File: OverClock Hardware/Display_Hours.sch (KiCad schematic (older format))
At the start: 40 parts, among them U3 10M02SCE144

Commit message: Completed Initial Routing
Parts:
- R11, R12, R13, R14, R15, R16, R17, R18, R19, R20, R21, R22, R23, R24, R25, R26: footprint Resistor_SMD:R_0805_2012Metric_Pad1.15x1.40mm_HandSolder -> Resistor_SMD:R_0603_1608Metric_Pad1.05x0.95mm_HandSolder
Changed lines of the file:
@@
 F 0 "R11" H 10909 5346 50  0000 L CNN
 F 1 "1K" H 10909 5255 50  0000 L CNN
-F 2 "Resistor_SMD:R_0805_2012Metric_Pad1.15x1.40mm_HandSolder" H 10850 5300 50  0001 C CNN
+F 2 "Resistor_SMD:R_0603_1608Metric_Pad1.05x0.95mm_HandSolder" H 10850 5300 50  0001 C CNN
 F 3 "~" H 10850 5300 50  0001 C CNN
 	1    10850 5300
@@
 F 0 "R12" H 11459 5346 50  0000 L CNN
 F 1 "1K" H 11459 5255 50  0000 L CNN
-F 2 "Resistor_SMD:R_0805_2012Metric_Pad1.15x1.40mm_HandSolder" H 11400 5300 50  0001 C CNN
+F 2 "Resistor_SMD:R_0603_1608Metric_Pad1.05x0.95mm_HandSolder" H 11400 5300 50  0001 C CNN
 F 3 "~" H 11400 5300 50  0001 C CNN
 	1    11400 5300
@@
 F 0 "R13" H 12009 5346 50  0000 L CNN
 F 1 "1K" H 12009 5255 50  0000 L CNN
-F 2 "Resistor_SMD:R_0805_2012Metric_Pad1.15x1.40mm_HandSolder" H 11950 5300 50  0001 C CNN
+F 2 "Resistor_SMD:R_0603_1608Metric_Pad1.05x0.95mm_HandSolder" H 11950 5300 50  0001 C CNN
 F 3 "~" H 11950 5300 50  0001 C CNN
 	1    11950 5300
@@
 F 0 "R14" H 12559 5346 50  0000 L CNN
 F 1 "1K" H 12559 5255 50  0000 L CNN
-F 2 "Resistor_SMD:R_0805_2012Metric_Pad1.15x1.40mm_HandSolder" H 12500 5300 50  0001 C CNN
+F 2 "Resistor_SMD:R_0603_1608Metric_Pad1.05x0.95mm_HandSolder" H 12500 5300 50  0001 C CNN
 F 3 "~" H 12500 5300 50  0001 C CNN
 	1    12500 5300
@@
 F 0 "R15" H 13109 5346 50  0000 L CNN
 F 1 "1K" H 13109 5255 50  0000 L CNN
-F 2 "Resistor_SMD:R_0805_2012Metric_Pad1.15x1.40mm_HandSolder" H 13050 5300 50  0001 C CNN
+F 2 "Resistor_SMD:R_0603_1608Metric_Pad1.05x0.95mm_HandSolder" H 13050 5300 50  0001 C CNN
 F 3 "~" H 13050 5300 50  0001 C CNN
 	1    13050 5300
@@
 F 0 "R16" H 13659 5346 50  0000 L CNN
 F 1 "1K" H 13659 5255 50  0000 L CNN
-F 2 "Resistor_SMD:R_0805_2012Metric_Pad1.15x1.40mm_HandSolder" H 13600 5300 50  0001 C CNN
+F 2 "Resistor_SMD:R_0603_1608Metric_Pad1.05x0.95mm_HandSolder" H 13600 5300 50  0001 C CNN
 F 3 "~" H 13600 5300 50  0001 C CNN
 	1    13600 5300
@@
 F 0 "R17" H 14209 5346 50  0000 L CNN
 F 1 "1K" H 14209 5255 50  0000 L CNN
-F 2 "Resistor_SMD:R_0805_2012Metric_Pad1.15x1.40mm_HandSolder" H 14150 5300 50  0001 C CNN
+F 2 "Resistor_SMD:R_0603_1608Metric_Pad1.05x0.95mm_HandSolder" H 14150 5300 50  0001 C CNN
 F 3 "~" H 14150 5300 50  0001 C CNN
 	1    14150 5300
@@
 F 0 "R18" H 14809 5346 50  0000 L CNN
 F 1 "1K" H 14809 5255 50  0000 L CNN
-F 2 "Resistor_SMD:R_0805_2012Metric_Pad1.15x1.40mm_HandSolder" H 14750 5300 50  0001 C CNN
+F 2 "Resistor_SMD:R_0603_1608Metric_Pad1.05x0.95mm_HandSolder" H 14750 5300 50  0001 C CNN
 F 3 "~" H 14750 5300 50  0001 C CNN
 	1    14750 5300
@@
 F 0 "R19" H 3759 5396 50  0000 L CNN
 F 1 "1K" H 3759 5305 50  0000 L CNN
-F 2 "Resistor_SMD:R_0805_2012Metric_Pad1.15x1.40mm_HandSolder" H 3700 5350 50  0001 C CNN
+F 2 "Resistor_SMD:R_0603_1608Metric_Pad1.05x0.95mm_HandSolder" H 3700 5350 50  0001 C CNN
 F 3 "~" H 3700 5350 50  0001 C CNN
 	1    3700 5350
@@
 F 0 "R20" H 4309 5396 50  0000 L CNN
 F 1 "1K" H 4309 5305 50  0000 L CNN
-F 2 "Resistor_SMD:R_0805_2012Metric_Pad1.15x1.40mm_HandSolder" H 4250 5350 50  0001 C CNN
+F 2 "Resistor_SMD:R_0603_1608Metric_Pad1.05x0.95mm_HandSolder" H 4250 5350 50  0001 C CNN
 F 3 "~" H 4250 5350 50  0001 C CNN
 	1    4250 5350
@@
 F 0 "R21" H 4859 5396 50  0000 L CNN
 F 1 "1K" H 4859 5305 50  0000 L CNN
-F 2 "Resistor_SMD:R_0805_2012Metric_Pad1.15x1.40mm_HandSolder" H 4800 5350 50  0001 C CNN
+F 2 "Resistor_SMD:R_0603_1608Metric_Pad1.05x0.95mm_HandSolder" H 4800 5350 50  0001 C CNN
 F 3 "~" H 4800 5350 50  0001 C CNN
 	1    4800 5350
@@
 F 0 "R22" H 5409 5396 50  0000 L CNN
 F 1 "1K" H 5409 5305 50  0000 L CNN
-F 2 "Resistor_SMD:R_0805_2012Metric_Pad1.15x1.40mm_HandSolder" H 5350 5350 50  0001 C CNN
+F 2 "Resistor_SMD:R_0603_1608Metric_Pad1.05x0.95mm_HandSolder" H 5350 5350 50  0001 C CNN
 F 3 "~" H 5350 5350 50  0001 C CNN
 	1    5350 5350
@@
 F 0 "R23" H 5959 5396 50  0000 L CNN
 F 1 "1K" H 5959 5305 50  0000 L CNN
-F 2 "Resistor_SMD:R_0805_2012Metric_Pad1.15x1.40mm_HandSolder" H 5900 5350 50  0001 C CNN
+F 2 "Resistor_SMD:R_0603_1608Metric_Pad1.05x0.95mm_HandSolder" H 5900 5350 50  0001 C CNN
 F 3 "~" H 5900 5350 50  0001 C CNN
 	1    5900 5350
@@
 F 0 "R24" H 6509 5396 50  0000 L CNN
 F 1 "1K" H 6509 5305 50  0000 L CNN
-F 2 "Resistor_SMD:R_0805_2012Metric_Pad1.15x1.40mm_HandSolder" H 6450 5350 50  0001 C CNN
+F 2 "Resistor_SMD:R_0603_1608Metric_Pad1.05x0.95mm_HandSolder" H 6450 5350 50  0001 C CNN
 F 3 "~" H 6450 5350 50  0001 C CNN
 	1    6450 5350
@@
 F 0 "R25" H 7059 5396 50  0000 L CNN
 F 1 "1K" H 7059 5305 50  0000 L CNN
-F 2 "Resistor_SMD:R_0805_2012Metric_Pad1.15x1.40mm_HandSolder" H 7000 5350 50  0001 C CNN
+F 2 "Resistor_SMD:R_0603_1608Metric_Pad1.05x0.95mm_HandSolder" H 7000 5350 50  0001 C CNN
 F 3 "~" H 7000 5350 50  0001 C CNN
 	1    7000 5350
@@
 F 0 "R26" H 7659 5396 50  0000 L CNN
 F 1 "1K" H 7659 5305 50  0000 L CNN
-F 2 "Resistor_SMD:R_0805_2012Metric_Pad1.15x1.40mm_HandSolder" H 7600 5350 50  0001 C CNN
+F 2 "Resistor_SMD:R_0603_1608Metric_Pad1.05x0.95mm_HandSolder" H 7600 5350 50  0001 C CNN
 F 3 "~" H 7600 5350 50  0001 C CNN
 	1    7600 5350

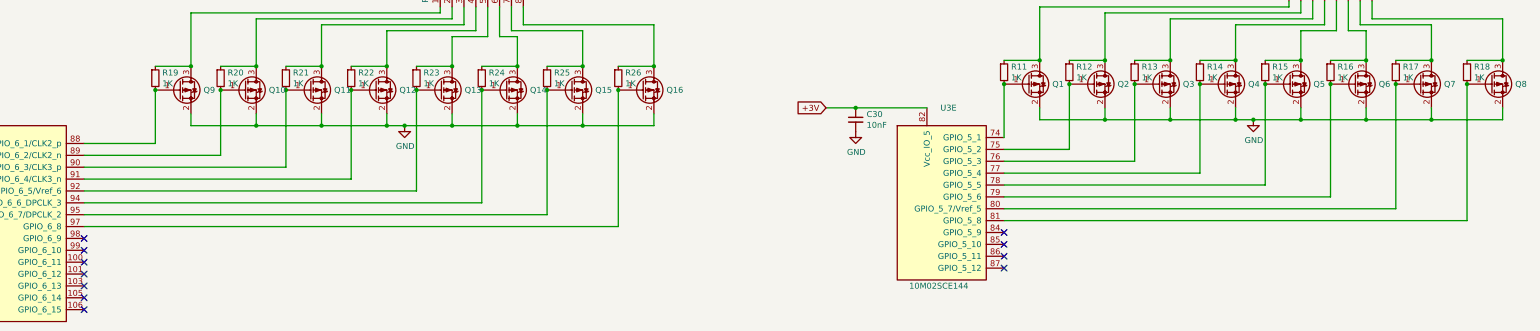
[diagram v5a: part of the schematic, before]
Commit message: Rerouted 7 Segment Displays
Rearranged the displays for cleaner routing, also modified the schematic for some of the displays to allow for better routing.
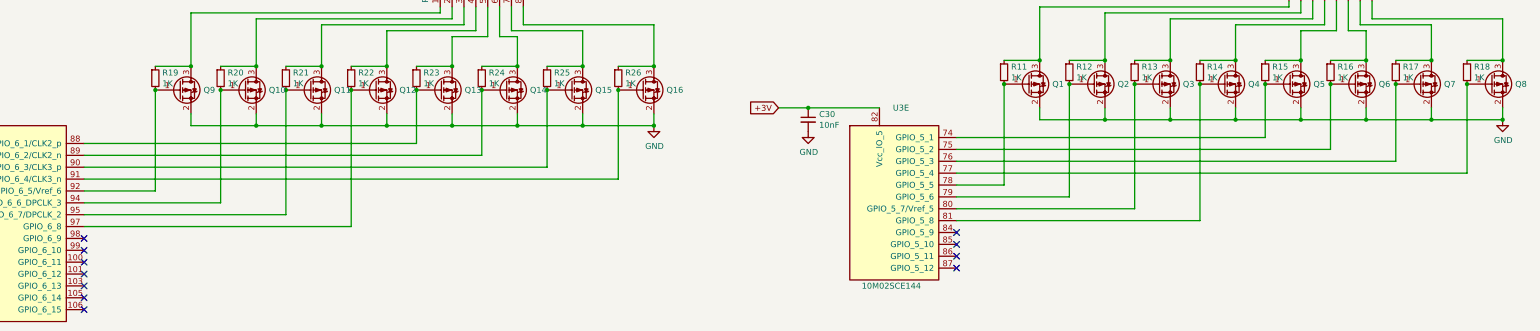
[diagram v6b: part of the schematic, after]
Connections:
- net at Q1.1 (G), R11.2: now also U3.78 (GPIO_5_5); no longer U3.74 (GPIO_5_1)
- net at Q2.1 (G), R12.2: now also U3.79 (GPIO_5_6); no longer U3.75 (GPIO_5_2)
- net at Q3.1 (G), R13.2: now also U3.80 (GPIO_5_7/Vref_5); no longer U3.76 (GPIO_5_3)
- net at Q4.1 (G), R14.2: now also U3.81 (GPIO_5_8); no longer U3.77 (GPIO_5_4)
- net at Q5.1 (G), R15.2: now also U3.74 (GPIO_5_1); no longer U3.78 (GPIO_5_5)
- net at Q6.1 (G), R16.2: now also U3.75 (GPIO_5_2); no longer U3.79 (GPIO_5_6)
- net at Q7.1 (G), R17.2: now also U3.76 (GPIO_5_3); no longer U3.80 (GPIO_5_7/Vref_5)
- net at Q8.1 (G), R18.2: now also U3.77 (GPIO_5_4); no longer U3.81 (GPIO_5_8)
- net at Q10.1 (G), R20.2: now also U3.94 (GPIO_6_6_DPCLK_3); no longer U3.89 (GPIO_6_2/CLK2_n)
- net at Q9.1 (G), R19.2: now also U3.92 (GPIO_6_5/Vref_6); no longer U3.88 (GPIO_6_1/CLK2_p)
- net at Q11.1 (G), R21.2: now also U3.95 (GPIO_6_7/DPCLK_2); no longer U3.90 (GPIO_6_3/CLK3_p)
- net at Q12.1 (G), R22.2: now also U3.97 (GPIO_6_8); no longer U3.91 (GPIO_6_4/CLK3_n)
- net at Q13.1 (G), R23.2: now also U3.88 (GPIO_6_1/CLK2_p); no longer U3.92 (GPIO_6_5/Vref_6)
- net at Q14.1 (G), R24.2: now also U3.89 (GPIO_6_2/CLK2_n); no longer U3.94 (GPIO_6_6_DPCLK_3)
- net at Q15.1 (G), R25.2: now also U3.90 (GPIO_6_3/CLK3_p); no longer U3.95 (GPIO_6_7/DPCLK_2)
- net at Q16.1 (G), R26.2: now also U3.91 (GPIO_6_4/CLK3_n); no longer U3.97 (GPIO_6_8)
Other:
- moved on the sheet: C30, U3E
